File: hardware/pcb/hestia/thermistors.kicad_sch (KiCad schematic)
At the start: 60 parts, among them J10 B2B-ZR, J11 B2B-ZR, J12 B2B-ZR, J13 B2B-ZR, J14 B2B-ZR, J15 B2B-ZR, J16 B2B-ZR, J7 B2B-ZR, J8 B2B-ZR, J9 B2B-ZR, U4 MAX31725MTA+T, U5 MAX31725MTA+T, U6 MAX31725MTA+T, U7 MAX31725MTA+T

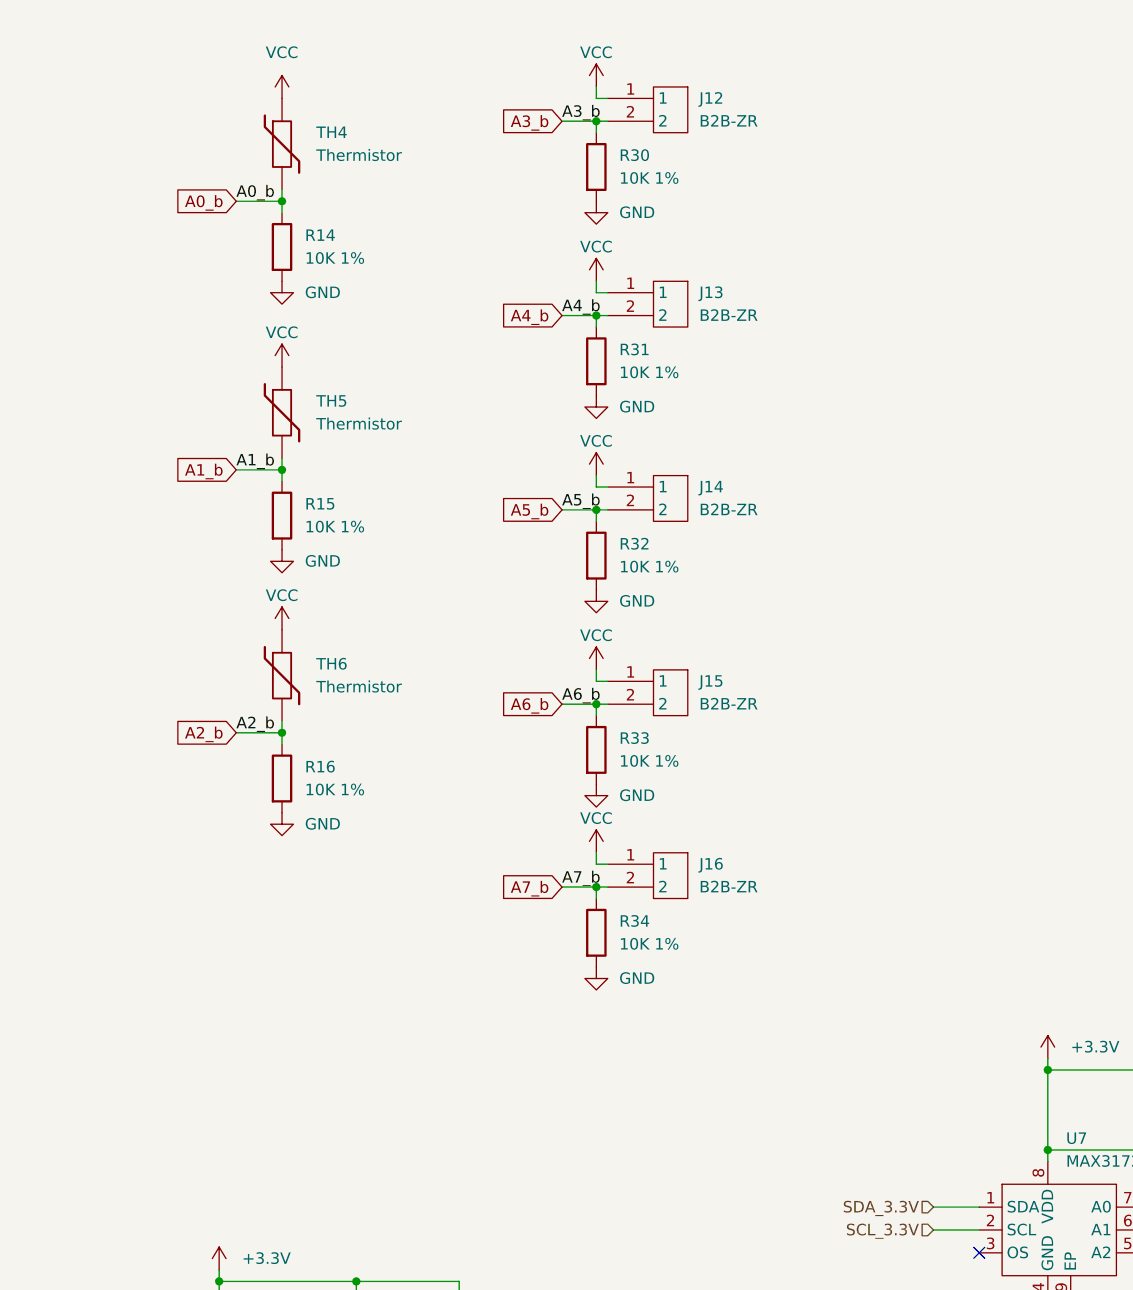
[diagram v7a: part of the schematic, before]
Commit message: add ferrite chipbeads to u3. add capacitor to u3 adc ref. add capacitor to u3 thermistor input top side 3.3V supply side of resistor divider.
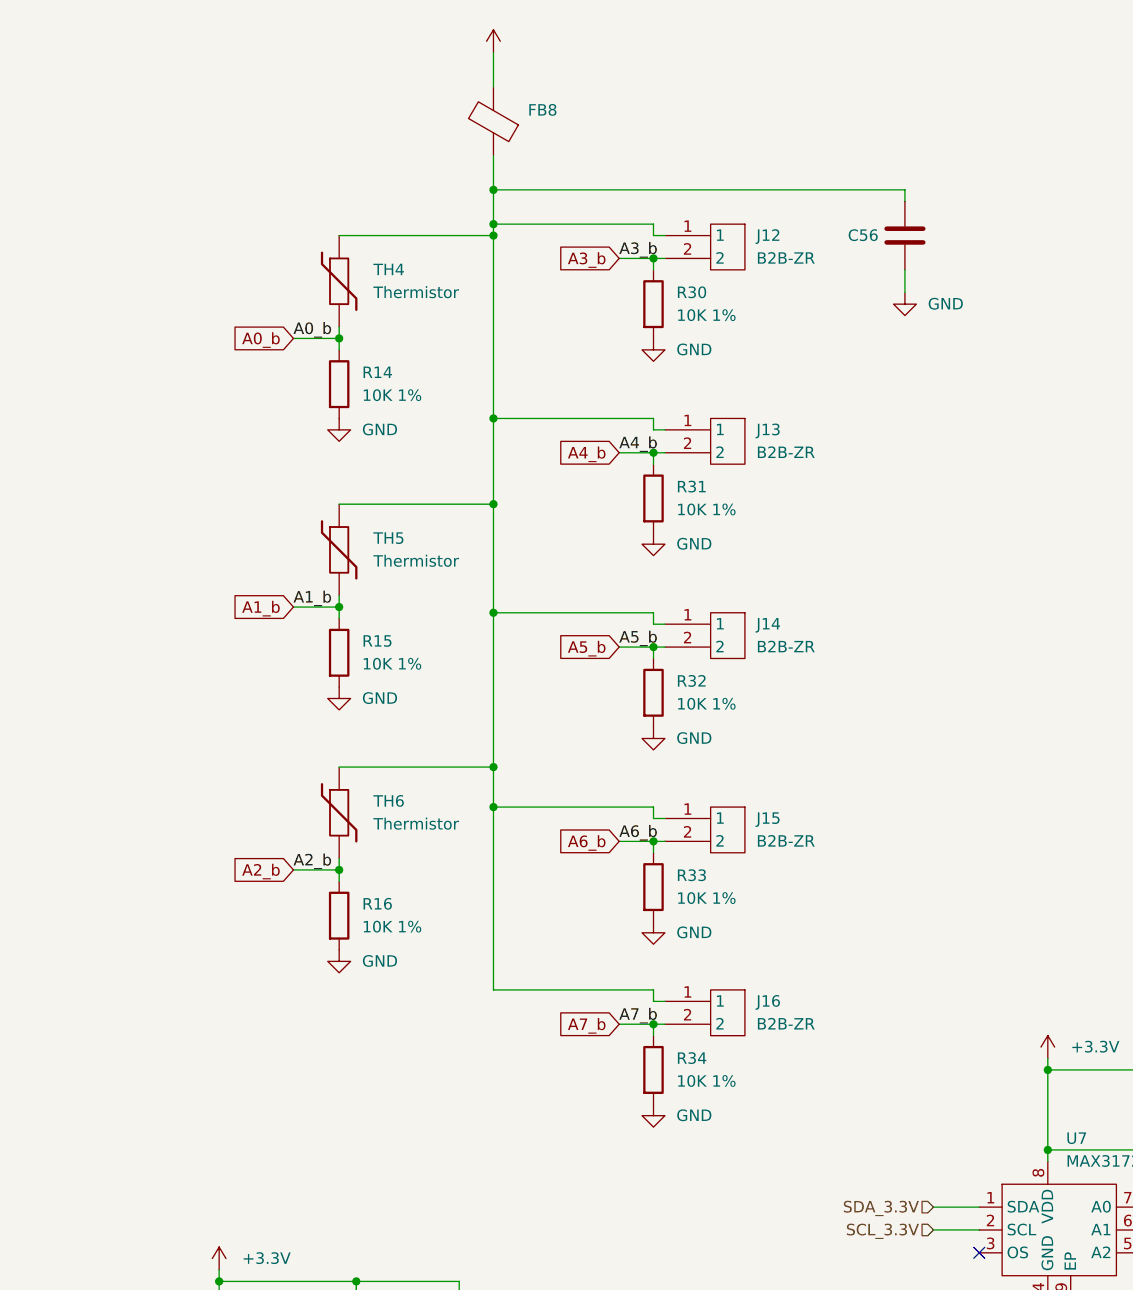
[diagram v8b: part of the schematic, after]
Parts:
- added C56: (no value), symbol Device:C
- added FB8: (no value), symbol Device:FerriteBead
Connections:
- net +3V3: now also FB8.2
- net GND: now also C56.2
- net VCC: no longer names the net of J12.1, J13.1, J14.1, J15.1, J16.1, TH4.1, TH5.1, TH6.1
- net VCC: now also C56.1, FB8.1
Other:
- moved on the sheet: J12, J13, J14, J15, J16, R14, R15, R16, R30, R31, R32, R33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
